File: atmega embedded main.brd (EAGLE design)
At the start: 354.1 x 155.8 mm, 148 parts, among them K1 SWITCH, K10 SWITCH, K11 SWITCH, K12 SWITCH, K13 SWITCH, K14 SWITCH, K15 SWITCH, K16 SWITCH, K17 SWITCH, K18 SWITCH, K19 SWITCH, K2 SWITCH, K20 SWITCH, K21 SWITCH, K22 SWITCH, K23 SWITCH, K24 SWITCH, K25 SWITCH, K26 SWITCH, K27 SWITCH, K28 SWITCH, K29 SWITCH, K3 SWITCH, K30 SWITCH, K31 SWITCH, K32 SWITCH, K33 SWITCH, K34 SWITCH, K35 SWITCH, K36 SWITCH, K37 SWITCH, K38 SWITCH, K39 SWITCH, K4 SWITCH, K40 SWITCH, K41 SWITCH, K42 SWITCH, K43 SWITCH, K44 SWITCH, K45 SWITCH, K46 SWITCH, K47 SWITCH, K48 SWITCH, K49 SWITCH, K5 SWITCH, K50 SWITCH, K51 SWITCH, K52 SWITCH, K53 SWITCH, K54 SWITCH, K55 SWITCH, K56 SWITCH, K57 SWITCH, K58 SWITCH, K59 SWITCH, K6 SWITCH, K60 SWITCH, K61 SWITCH, K62 SWITCH, K63 SWITCH, K64 SWITCH, K65 SWITCH, K66 SWITCH, K7 SWITCH, K8 SWITCH, K9 SWITCH, U1 ATMEGA32U4-AU, X1 XTAL_GND

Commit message: Replaced chip with Atmege328p and made some other adjustments to the schematic
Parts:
- removed D45: (no value), adafruit:DO-1N4148
- removed D63: (no value), adafruit:SMADIODE
- removed K60: SWITCH, keyboard_switch:KAILH_LOW_PROFILE
- added C10, C9: 22p, adafruit:C0805
- added CN2: (no value), adafruit:USB-MINIB
- added D29: (no value), adafruit:SMADIODE
- added IC1: ATMEGA328PROUND, atmega328:DIL28-3-ROUND
- added R5: 10K, adafruit:M0805
- added R6, R7: 22, adafruit:M0805
- added SW2: (no value), adafruit:PUSHBUTTON_SMD_SJ
- added X2: XTAL_GND, adafruit:NX3225
- moved D15 342.0 mm to (-10.8, -114.8), flipped to the top
- moved K47 340.2 mm to (-4.40, -130.4), flipped to the top
- moved K24 147.0 mm to (-4.40, -102.8), flipped to the top
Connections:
- removed net N$43: D45.C, K24.P$2
- removed net N$65: D63.C, K60.P$2
- removed net N$80: D15.C, K47.P$2
- new net D+: CN2.D+, IC1.23, R6.1, R6.2
- new net D-: CN2.D-, R7.2
- new net N$15: IC1.1, R5.2, SW2.P$2
- new net N$16: C9.1, IC1.9, X2.1
- new net N$17: C10.1, IC1.10, X2.3
- new net N$19: D15.C, K24.P$2
- new net N$20: D29.C, K47.P$2
- new net N$21: IC1.24, R7.1
- new net N$22: CN2.ID
- net COL10: now also K62.P$1
- net COL13: no longer K60.P$1
- net COL14: no longer K47.P$1
- net COL3: no longer K24.P$1
- net COL6: now also K47.P$1
- net COL8: now also K24.P$1
- net COL9: no longer K62.P$1
- net G1: now also X2.4
- net GND: now also C10.2, C9.2, CN2.GND, IC1.22, IC1.8, SW2.P$1, X2.2
- net ROW1: now also D15.A, D29.A
- net ROW2: no longer D45.A, D63.A
- net ROW4: no longer D15.A
- net VCC: now also CN2.VBUS, IC1.20, IC1.21, IC1.7, R5.1
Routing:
- net N$80: track 7.45 -> 0.00 mm
- net N$65: track 7.45 -> 0.00 mm
- net N$18: track 7.45 -> 0.00 mm
- net COL2: track 101.4 -> 95.4 mm

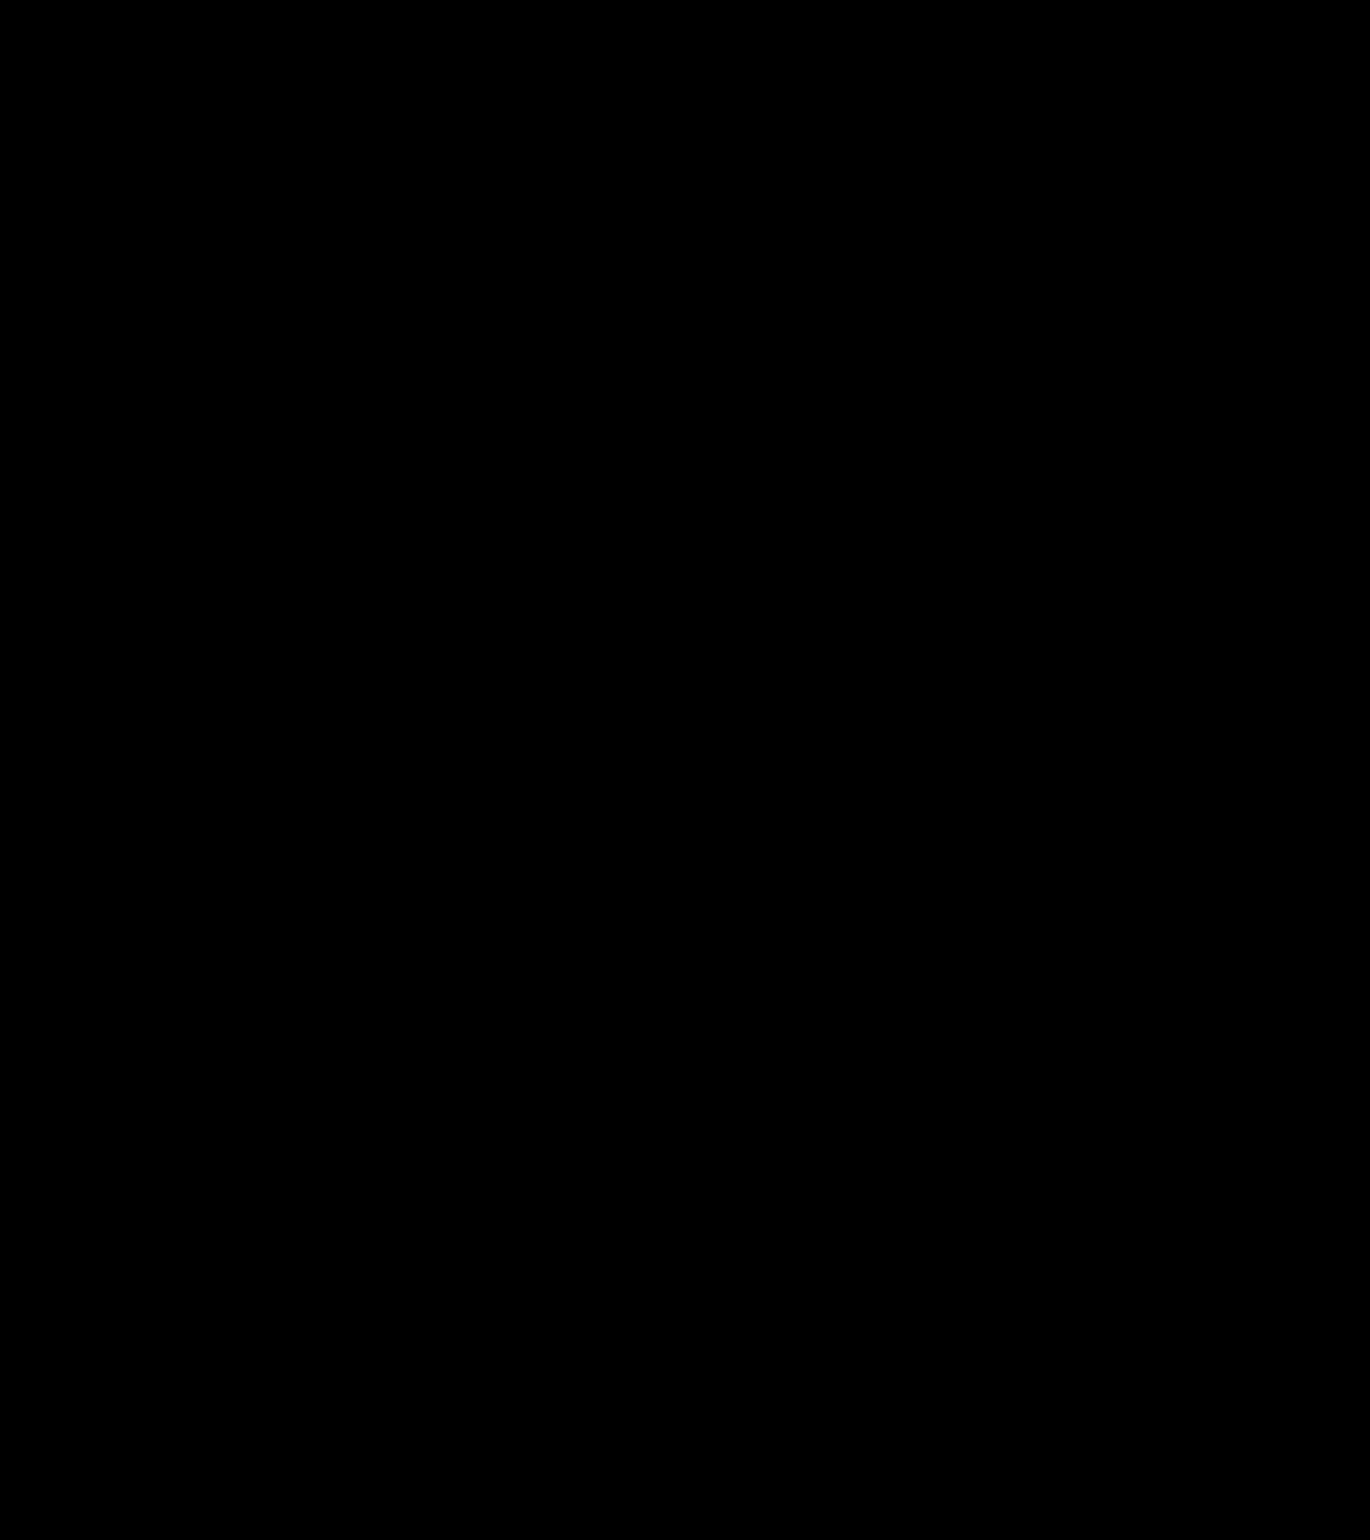
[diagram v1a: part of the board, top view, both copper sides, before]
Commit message: Added an alternative wiring with fake rows for a chip with fewer pins
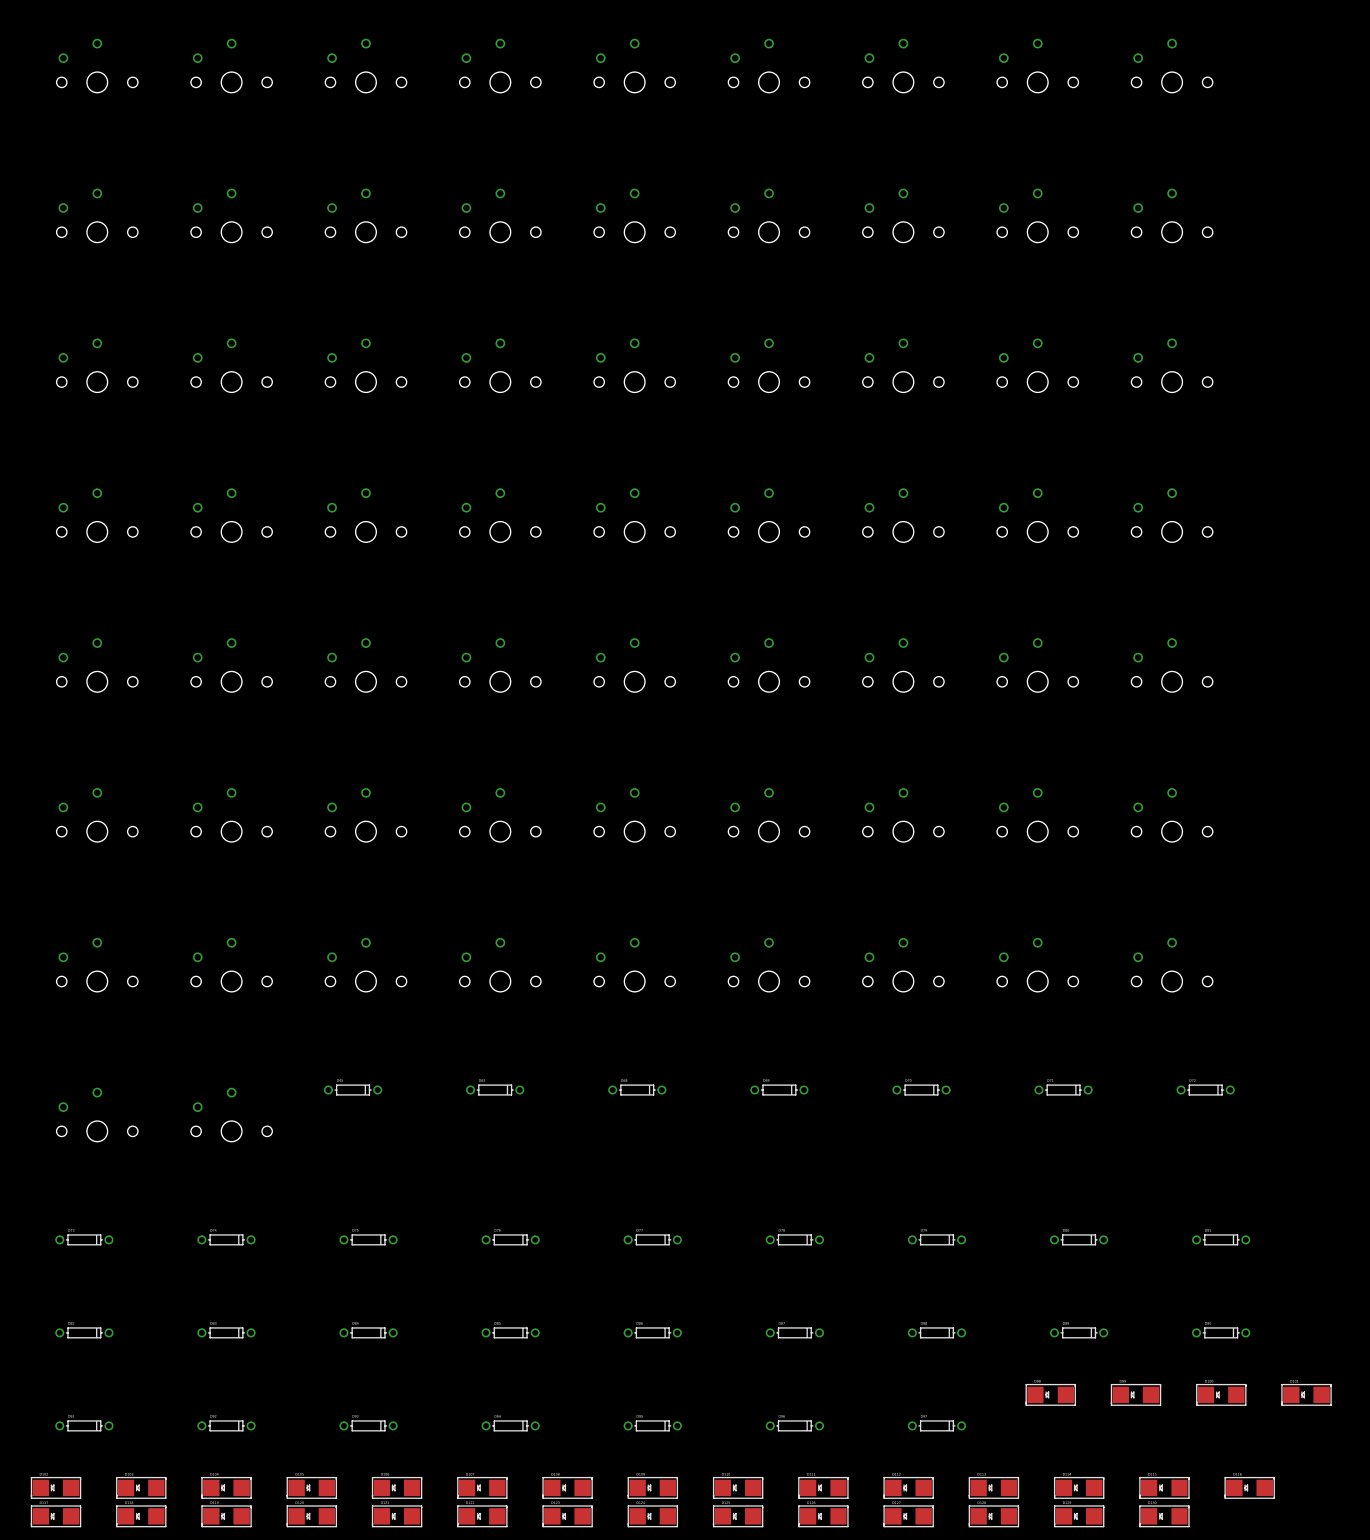
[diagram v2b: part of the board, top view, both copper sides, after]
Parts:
- added D100, D101, D102, D103, D104, D105, D106, D107, D108, D109, D110, D111, D112, D113, D114, D115, D116, D117, D118, D119, D120, D121, D122, D123, D124, D125, D126, D127, D128, D129, D130, D98, D99: (no value), adafruit:SMADIODE
- added D45, D63, D68, D69, D70, D71, D72, D73, D74, D75, D76, D77, D78, D79, D80, D81, D82, D83, D84, D85, D86, D87, D88, D89, D90, D91, D92, D93, D94, D95, D96, D97: (no value), adafruit:DO-1N4148
- added K100, K101, K102, K103, K104, K105, K106, K107, K108, K109, K110, K111, K112, K113, K114, K115, K116, K117, K118, K119, K120, K121, K122, K123, K124, K125, K126, K127, K128, K129, K130, K60, K67, K68, K69, K70, K71, K72, K73, K74, K75, K76, K77, K78, K79, K80, K81, K82, K83, K84, K85, K86, K87, K88, K89, K90, K91, K92, K93, K94, K95, K96, K97, K98, K99: SWITCH, keyboard_switch:KAILH_LOW_PROFILE
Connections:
- new net N$100: D71.C, K71.P$2
- new net N$101: D74.C, K78.P$2
- new net N$102: D116.C, K98.P$1
- new net N$103: D117.C, K105.P$1
- new net N$104: D95.C, K85.P$2
- new net N$105: D94.C, K91.P$2
- new net N$106: D104.C, K128.P$2
- new net N$107: D86.C, K97.P$2
- new net N$108: D93.C, K90.P$2
- new net N$109: D92.C, K84.P$2
- new net N$110: D75.C, K77.P$2
- new net N$111: D115.C, K104.P$2
- new net N$112: D127.C, K123.P$2
- new net N$113: D111.C, K124.P$2
- new net N$114: D126.C, K121.P$2
- new net N$115: D120.C, K120.P$2
- new net N$116: D128.C, K117.P$2
- new net N$118: D114.C, K127.P$2
- new net N$119: D113.C, K126.P$2
- new net N$120: D112.C, K125.P$2
- new net N$121: D119.C, K119.P$2
- new net N$123: D99.C, K99.P$2
- new net N$124: D100.C, K100.P$2
- new net N$125: D101.C, K101.P$2
- new net N$126: D102.C, K102.P$2
- new net N$127: D103.C, K103.P$2
- new net N$130: D124.C, K116.P$2
- new net N$131: D123.C, K115.P$2
- new net N$132: D122.C, K114.P$2
- new net N$133: D121.C, K113.P$2
- new net N$134: D118.C, K112.P$2
- new net N$135: D109.C, K106.P$2
- new net N$136: D108.C, K107.P$2
- new net N$137: D107.C, K108.P$2
- new net N$138: D106.C, K109.P$2
- new net N$139: D105.C, K110.P$2
- new net N$141: D63.C, K67.P$2
- new net N$142: D125.C, K122.P$2
- new net N$143: D129.C, K129.P$1
- new net N$144: D130.C, K130.P$2
- new net N$151: D82.C, K93.P$1
- new net N$152: D81.C, K87.P$1
- new net N$153: D80.C, K80.P$1
- new net N$154: D105.A, D106.A, D107.A, D108.A, D109.A
- new net N$155: D100.A, D101.A, D102.A, D103.A, D99.A
- new net N$160: D87.A, D90.A, D93.A, D94.A
- new net N$161: D72.C, K72.P$2
- new net N$162: D73.C, K79.P$2
- new net N$163: D96.C, K86.P$2
- new net N$164: D97.C, K92.P$2
- new net N$23: D45.C, K60.P$1
- new net N$24: D83.C, K94.P$2
- new net N$25: D79.C, K73.P$1
- new net N$26: D118.A, D121.A, D122.A, D123.A, D124.A
- new net N$27: D98.C, K118.P$1
- new net N$28: D110.C, K111.P$1
- new net N$35: D78.C, K74.P$2
- new net N$43: D77.C, K75.P$2
- new net N$64: D68.C, K68.P$2
- new net N$65: D89.C, K82.P$2
- new net N$72: D88.C, K81.P$2
- new net N$80: D87.C, K88.P$2
- new net N$92: D84.C, K95.P$2
- new net N$93: D85.C, K96.P$2
- new net N$94: D90.C, K89.P$2
- new net N$95: D91.C, K83.P$2
- new net N$96: D76.C, K76.P$2
- new net N$97: D69.C, K69.P$2
- new net N$98: D70.C, K70.P$2
- new net ROW6: D104.A, D115.A, D127.A, D128.A, D45.A, D79.A, D80.A, D81.A, D82.A
- new net ROW7: D110.A, D116.A, D117.A, D72.A, D73.A, D96.A, D97.A, D98.A
- net COL10: now also K100.P$1, K107.P$1, K111.P$2, K113.P$1, K120.P$1, K124.P$1, K128.P$1
- net COL11: now also K101.P$1, K105.P$2, K108.P$1, K114.P$1, K121.P$1, K123.P$1, K125.P$1
- net COL12: now also K102.P$1, K109.P$1, K115.P$1, K117.P$1, K122.P$1, K126.P$1, K98.P$2
- net COL13: now also K103.P$1, K104.P$1, K110.P$1, K116.P$1, K127.P$1
- net COL2: now also K60.P$2, K67.P$1, K74.P$1, K81.P$1, K88.P$1, K94.P$1
- net COL3: now also K68.P$1, K72.P$1, K73.P$2, K75.P$1, K82.P$1, K95.P$1
- net COL4: now also K69.P$1, K76.P$1, K79.P$1, K80.P$2, K83.P$1, K89.P$1, K96.P$1
- net COL5: now also K70.P$1, K77.P$1, K84.P$1, K86.P$1, K87.P$2, K90.P$1, K97.P$1
- net COL6: now also K130.P$1, K71.P$1, K78.P$1, K85.P$1, K91.P$1, K92.P$1, K93.P$2
- net COL9: now also K106.P$1, K112.P$1, K118.P$2, K119.P$1, K129.P$2, K99.P$1
- net ROW1: now also D63.A, D68.A, D69.A, D70.A, D71.A
- net ROW2: now also D74.A, D75.A, D76.A, D77.A, D78.A
- net ROW3: now also D88.A, D89.A, D91.A, D92.A, D95.A
- net ROW4: now also D119.A, D120.A, D125.A, D126.A
- net ROW5: now also D111.A, D112.A, D113.A, D114.A, D129.A, D130.A, D83.A, D84.A, D85.A, D86.A

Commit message: Traced stuff
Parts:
- removed C1, C2: 22p, adafruit:C0805
- removed C8: 1u, adafruit:C0805
- removed CN1, CN2: (no value), adafruit:USB-MINIB
- removed D1, D2, D22, D23, D24, D25, D26, D27, D28, D3, D30, D31, D32, D33, D34, D35, D36, D4, D42, D43, D44, D46, D47, D48, D49, D5, D50, D51, D52, D53, D6, D7: (no value), adafruit:DO-1N4148
- removed D10, D11, D12, D13, D14, D15, D16, D17, D18, D19, D20, D21, D29, D37, D38, D39, D40, D41, D54, D55, D56, D57, D58, D59, D60, D61, D62, D64, D65, D66, D67, D8, D9: (no value), adafruit:SMADIODE
- removed K1, K10, K11, K12, K13, K14, K15, K16, K17, K18, K19, K2, K20, K21, K22, K23, K24, K25, K26, K27, K28, K29, K3, K30, K31, K32, K33, K34, K35, K36, K37, K38, K39, K4, K40, K41, K42, K43, K44, K45, K46, K47, K48, K49, K5, K50, K51, K52, K53, K54, K55, K56, K57, K58, K59, K6, K61, K62, K63, K64, K65, K66, K7, K8, K9: SWITCH, keyboard_switch:KAILH_LOW_PROFILE
- removed R1, R2: 10K, adafruit:M0805
- removed R3, R4: 22, adafruit:M0805
- removed SW1, SW2: (no value), adafruit:PUSHBUTTON_SMD_SJ
- removed X1, X2: XTAL_GND, adafruit:NX3225
- added Q1: (no value), crystal:HC49/S
- added S1: (no value), switch-omron:B3F-10XX
- D45, D63, D68, D69, D70, D71, D72, D73, D74, D75, D76, D77, D78, D79, D80, D81, D82, D83, D84, D85, D86, D87, D88, D89, D90, D91, D92, D93, D94, D95, D96, D97: device adafruit:DO-1N4148 -> adafruit:SMADIODE
- U1: value ATMEGA32U4-AU -> (none); device adafruit:TQFP44 -> microusb:USB-MICRO-SMD
- moved D103 540.0 mm to (271.9, 80.8)
- moved D102 537.7 mm to (254.1, 80.8)
- moved D105 510.8 mm to (272.5, 61.8)
- moved D106 496.5 mm to (254.1, 61.8)
- moved D117 490.7 mm to (165.1, 66.5), turned to 180 degrees
- moved D115 489.7 mm to (288.6, 85.5), turned to 180 degrees
- moved D107 483.7 mm to (235.1, 61.8)
- moved D104 481.5 mm to (288.6, 9.50), turned to 180 degrees
- moved D118 476.0 mm to (197.1, 42.8)
- moved D124 474.5 mm to (272.5, 42.8)
- moved D128 474.4 mm to (288.6, 57.0), turned to 180 degrees
- moved D116 472.8 mm to (165.1, 85.5), turned to 180 degrees
- moved D108 472.6 mm to (216.1, 61.8)
- moved D123 472.4 mm to (254.1, 42.8)
- moved D122 470.1 mm to (235.1, 42.8)
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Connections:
- removed net COL11: K101.P$1, K105.P$2, K108.P$1, K114.P$1, K121.P$1, K123.P$1, K125.P$1, K37.P$1, K44.P$1, K51.P$1, K58.P$1, K63.P$1, U1.12
- removed net COL12: K102.P$1, K109.P$1, K115.P$1, K117.P$1, K122.P$1, K126.P$1, K38.P$1, K45.P$1, K52.P$1, K59.P$1, K64.P$1, K98.P$2, U1.36
- removed net COL13: K103.P$1, K104.P$1, K110.P$1, K116.P$1, K127.P$1, K39.P$1, K46.P$1, K53.P$1, K65.P$1, U1.37
- removed net COL14: K40.P$1, K54.P$1, K61.P$1, K66.P$1, U1.38
- removed net G1: X1.4, X2.4
- removed net N$1 (its old number): C1.1, U1.17, X1.1
- removed net N$100: D71.C, K71.P$2
- removed net N$101: D74.C, K78.P$2
- removed net N$102: D116.C, K98.P$1
- removed net N$103: D117.C, K105.P$1
- removed net N$104: D95.C, K85.P$2
- removed net N$105: D94.C, K91.P$2
- removed net N$107: D86.C, K97.P$2
- removed net N$108: D93.C, K90.P$2
- removed net N$109: D92.C, K84.P$2
- removed net N$110: D75.C, K77.P$2
- removed net N$113: D111.C, K124.P$2
- removed net N$114: D126.C, K121.P$2
- removed net N$115: D120.C, K120.P$2
- removed net N$118: D114.C, K127.P$2
- removed net N$119: D113.C, K126.P$2
- removed net N$120: D112.C, K125.P$2
- removed net N$121: D119.C, K119.P$2
- removed net N$123: D99.C, K99.P$2
- removed net N$124: D100.C, K100.P$2
- removed net N$125: D101.C, K101.P$2
- removed net N$126: D102.C, K102.P$2
- removed net N$127: D103.C, K103.P$2
- removed net N$130: D124.C, K116.P$2
- removed net N$131: D123.C, K115.P$2
- removed net N$132: D122.C, K114.P$2
- removed net N$133: D121.C, K113.P$2
- removed net N$134: D118.C, K112.P$2
- removed net N$135: D109.C, K106.P$2
- removed net N$136: D108.C, K107.P$2
- removed net N$137: D107.C, K108.P$2
- removed net N$138: D106.C, K109.P$2
- removed net N$139: D105.C, K110.P$2
- removed net N$141: D63.C, K67.P$2
- removed net N$144: D130.C, K130.P$2
- removed net N$154: D105.A, D106.A, D107.A, D108.A, D109.A
- removed net N$155: D100.A, D101.A, D102.A, D103.A, D99.A
- removed net N$160: D87.A, D90.A, D93.A, D94.A
- removed net N$161: D72.C, K72.P$2
- removed net N$162: D73.C, K79.P$2
- removed net N$163: D96.C, K86.P$2
- removed net N$164: D97.C, K92.P$2
- removed net N$2 (its old number): C2.1, U1.16, X1.3
- removed net N$26 (its old number): D118.A, D121.A, D122.A, D123.A, D124.A
- removed net N$3 (its old number): R1.2, SW1.P$2, U1.13
- removed net N$4 (its old number): R2.2, U1.33
- removed net N$42: D34.C, K31.P$2
- removed net N$5 (its old number): CN1.D+, R3.1
- removed net N$65 (its old number): D89.C, K82.P$2
- removed net N$66 (its old number): D67.C, K61.P$2
- removed net N$67 (its old number): D41.C, K66.P$2
- removed net N$68 (its old number): D40.C, K65.P$2
- removed net N$69: D39.C, K64.P$2
- removed net N$70: D38.C, K63.P$2
- removed net N$71: D57.C, K56.P$2
- removed net N$72: D88.C, K81.P$2
- removed net N$73: D21.C, K41.P$2
- removed net N$74: D9.C, K35.P$2
- removed net N$75: D10.C, K36.P$2
- removed net N$76: D11.C, K37.P$2
- removed net N$77: D12.C, K38.P$2
- removed net N$78: D13.C, K39.P$2
- removed net N$79: D14.C, K40.P$2
- removed net N$81: D66.C, K54.P$2
- removed net N$82: D62.C, K53.P$2
- removed net N$83: D61.C, K52.P$2
- removed net N$84: D60.C, K51.P$2
- removed net N$85: D59.C, K50.P$2
- removed net N$86: D56.C, K49.P$2
- removed net N$87: D20.C, K42.P$2
- removed net N$88: D19.C, K43.P$2
- removed net N$89: D18.C, K44.P$2
- removed net N$90: D17.C, K45.P$2
- removed net N$91: D16.C, K46.P$2
- removed net N$92: D84.C, K95.P$2
- removed net N$93: D85.C, K96.P$2
- removed net N$94: D90.C, K89.P$2
- removed net N$95: D91.C, K83.P$2
- removed net N$96: D76.C, K76.P$2
- removed net N$97: D69.C, K69.P$2
- removed net N$98: D70.C, K70.P$2
- new net N$23: D86.C, K97.P$1
- new net N$25: D75.C, K77.P$1
- net COL1: now also K60.P$2, K67.P$2, K74.P$2, K81.P$2, K88.P$2, K94.P$2; no longer K1.P$1, K15.P$1, K22.P$1, K29.P$1, K8.P$1, U1.22
- net COL10: now also K103.P$2, K104.P$1, K110.P$2, K116.P$2, K127.P$2; no longer K100.P$1, K107.P$1, K111.P$2, K113.P$1, K120.P$1, K124.P$1, K128.P$1, K36.P$1, K43.P$1, K50.P$1, K57.P$1, K62.P$1, U1.30
- net COL2: now also K68.P$2, K72.P$2, K73.P$2, K75.P$2, K82.P$2, K95.P$2; no longer K16.P$1, K2.P$1, K23.P$1, K30.P$1, K60.P$2, K67.P$1, K74.P$1, K81.P$1, K88.P$1, K9.P$1, K94.P$1, U1.21
- net COL3: now also K69.P$2, K76.P$2, K79.P$2, K80.P$2, K83.P$2, K89.P$2, K96.P$2; no longer K10.P$1, K17.P$1, K3.P$1, K31.P$1, K68.P$1, K72.P$1, K73.P$2, K75.P$1, K82.P$1, K95.P$1, U1.20
- net COL4: now also K70.P$2, K77.P$2, K84.P$2, K86.P$2, K87.P$2, K90.P$2, K97.P$2; no longer K11.P$1, K18.P$1, K25.P$1, K32.P$1, K4.P$1, K69.P$1, K76.P$1, K79.P$1, K80.P$2, K83.P$1, K89.P$1, K96.P$1, U1.8
- net COL5: now also K130.P$2, K71.P$2, K78.P$2, K85.P$2, K91.P$2, K92.P$2, K93.P$2; no longer K12.P$1, K19.P$1, K26.P$1, K33.P$1, K5.P$1, K70.P$1, K77.P$1, K84.P$1, K86.P$1, K87.P$2, K90.P$1, K97.P$1, U1.9
- net COL6: now also K106.P$2, K112.P$2, K118.P$1, K119.P$2, K129.P$2, K99.P$2; no longer K13.P$1, K130.P$1, K20.P$1, K27.P$1, K47.P$1, K6.P$1, K71.P$1, K78.P$1, K85.P$1, K91.P$1, K92.P$1, K93.P$2, U1.10
- net COL7: now also K100.P$2, K107.P$2, K111.P$1, K113.P$2, K120.P$2, K124.P$2, K128.P$1; no longer K14.P$1, K21.P$1, K28.P$1, K7.P$1, U1.11
- net COL8: now also K101.P$2, K105.P$1, K108.P$2, K114.P$2, K121.P$2, K123.P$1, K125.P$2; no longer K24.P$1, K34.P$1, K41.P$1, K48.P$1, K55.P$1, U1.19
- net COL9: now also K102.P$2, K109.P$2, K115.P$2, K117.P$1, K122.P$2, K126.P$2, K98.P$1; no longer K106.P$1, K112.P$1, K118.P$2, K119.P$1, K129.P$2, K35.P$1, K42.P$1, K49.P$1, K56.P$1, K99.P$1, U1.18
- net D+: now also U1.D+1; no longer CN2.D+
- net D-: now also U1.D-1; no longer CN2.D-
- net GND: now also S1.4, U1.GND1; no longer C1.2, C2.2, C8.1, CN1.GND, CN2.GND, R2.1, SW1.P$1, SW2.P$1, U1.15, U1.23, U1.35, U1.43, U1.5, X1.2, X2.2
- net N$10: now also D77.C, K75.P$1; no longer D49.C, K26.P$2
- net N$11: now also D89.C, K82.P$1; no longer D48.C, K19.P$2
- net N$12: now also D68.C, K68.P$1; no longer D24.C, K12.P$2
- net N$13: now also D84.C, K95.P$1; no longer D8.C, K34.P$2
- net N$14: now also D76.C, K76.P$1; no longer D2.C, K2.P$2
- net N$142: now also K122.P$1; no longer K122.P$2
- net N$15: now also S1.1, S1.2; no longer SW2.P$2
- net N$16: now also Q1.2; no longer X2.1
- net N$17: now also Q1.1; no longer X2.3
- net N$18: now also D69.C, K69.P$1; no longer D64.C, K59.P$2
- net N$19: now also D90.C, K89.P$1; no longer D15.C, K24.P$2
- net N$20: now also D85.C, K96.P$1; no longer D29.C, K47.P$2
- net N$22: now also D91.C, K83.P$1; no longer CN2.ID
- net N$24: now also D70.C, K70.P$1; no longer D83.C, K94.P$2
- net N$27: now also K118.P$2; no longer K118.P$1
- net N$28: now also K111.P$2; no longer K111.P$1
- net N$29: now also D92.C, K84.P$1; no longer D32.C, K29.P$2
- net N$30: now also D93.C, K90.P$1; no longer D33.C, K30.P$2
- net N$31: now also D94.C, K91.P$1; no longer D31.C, K22.P$2
- net N$32: now also D71.C, K71.P$1; no longer D30.C, K15.P$2
- net N$33: now also D74.C, K78.P$1; no longer D28.C, K8.P$2
- net N$34: now also D95.C, K85.P$1; no longer D1.C, K1.P$2
- net N$35: now also D130.C, K130.P$1; no longer D78.C, K74.P$2
- net N$36: now also D72.C, K72.P$1; no longer D27.C, K9.P$2
- net N$37: now also D73.C, K79.P$1; no longer D26.C, K10.P$2
- net N$38: now also D96.C, K86.P$1; no longer D3.C, K3.P$2
- net N$39: now also D97.C, K92.P$1; no longer D44.C, K17.P$2
- net N$40: now also D117.C, K105.P$2; no longer D43.C, K16.P$2
- net N$41: now also D116.C, K98.P$2; no longer D42.C, K23.P$2
- net N$43: now also D119.C, K119.P$1; no longer D77.C, K75.P$2
- net N$44: now also D99.C, K99.P$1; no longer D35.C, K32.P$2
- net N$45: now also D109.C, K106.P$1; no longer D46.C, K25.P$2
- net N$46: now also D118.C, K112.P$1; no longer D47.C, K18.P$2
- net N$47: now also D111.C, K124.P$1; no longer D25.C, K11.P$2
- net N$48: now also D100.C, K100.P$1; no longer D4.C, K4.P$2
- net N$49: now also D108.C, K107.P$1; no longer D5.C, K5.P$2
- net N$50: now also D121.C, K113.P$1; no longer D7.C, K7.P$2
- net N$51: now also D120.C, K120.P$1; no longer D6.C, K6.P$2
- net N$52: now also D126.C, K121.P$1; no longer D23.C, K13.P$2
- net N$53: now also D101.C, K101.P$1; no longer D22.C, K14.P$2
- net N$54: now also D107.C, K108.P$1; no longer D52.C, K21.P$2
- net N$55: now also D122.C, K114.P$1; no longer D51.C, K20.P$2
- net N$56: now also D112.C, K125.P$1; no longer D50.C, K27.P$2
- net N$57: now also D123.C, K115.P$1; no longer D53.C, K28.P$2
- net N$58: now also D106.C, K109.P$1; no longer D54.C, K55.P$2
- net N$59: now also D102.C, K102.P$1; no longer D55.C, K48.P$2
- net N$6: now also D63.C, K67.P$1; no longer CN1.D-, R4.1
- net N$60: now also D113.C, K126.P$1; no longer D36.C, K33.P$2
- net N$61: now also D124.C, K116.P$1; no longer D37.C, K62.P$2
- net N$62: now also D105.C, K110.P$1; no longer D65.C, K58.P$2
- net N$63: now also D103.C, K103.P$1; no longer D58.C, K57.P$2
- net N$64: now also D114.C, K127.P$1; no longer D68.C, K68.P$2
- net N$7: now also D88.C, K81.P$1; no longer R4.2, U1.3
- net N$8: now also D78.C, K74.P$1; no longer R3.2, U1.4
- net N$80: now also K88.P$1; no longer K88.P$2
- net N$9: now also D83.C, K94.P$1; no longer C8.2, U1.6
- net ROW1: now also D100.A, D101.A, D102.A, D103.A, D99.A; no longer D15.A, D29.A, D32.A, D33.A, D34.A, D35.A, D36.A, D37.A, D38.A, D39.A, D40.A, D41.A, U1.29
- net ROW2: now also D105.A, D106.A, D107.A, D108.A, D109.A; no longer D31.A, D42.A, D46.A, D49.A, D50.A, D53.A, D54.A, D57.A, D58.A, D64.A, D65.A, D67.A, U1.28
- net ROW3: now also D118.A, D121.A, D122.A, D123.A, D124.A; no longer D30.A, D43.A, D44.A, D47.A, D48.A, D51.A, D52.A, D55.A, D56.A, D59.A, D60.A, D61.A, D62.A, D66.A, U1.27
- net ROW4: now also D87.A, D90.A, D93.A, D94.A; no longer D16.A, D17.A, D18.A, D19.A, D20.A, D21.A, D22.A, D23.A, D24.A, D25.A, D26.A, D27.A, D28.A, U1.26
- net ROW5: no longer D1.A, D10.A, D11.A, D12.A, D13.A, D14.A, D2.A, D3.A, D4.A, D5.A, D6.A, D7.A, D8.A, D9.A, U1.25
- net VCC: now also U1.VBUS1; no longer CN1.VBUS, CN2.VBUS, R1.1, U1.14, U1.2, U1.24, U1.34, U1.44
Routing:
- net ROW3: track 0.00 -> 369.7 mm
- net ROW5: track 114.2 -> 479.1 mm
- net ROW4: track 38.4 -> 389.8 mm, vias 2 -> 0
- net ROW2: track 0.00 -> 330.0 mm
- net ROW1: track 0.00 -> 262.2 mm
- net ROW6: track 0.00 -> 170.5 mm
- net ROW7: track 0.00 -> 119.7 mm
- net COL10: track 0.00 -> 110.5 mm
- net COL9: track 0.00 -> 109.5 mm
- net COL8: track 0.00 -> 104.0 mm
- net COL5: track 9.40 -> 111.2 mm, vias 1 -> 0
- net COL6: track 9.40 -> 104.4 mm, vias 1 -> 0
- net COL7: track 9.40 -> 104.0 mm, vias 1 -> 0
- net COL3: track 9.40 -> 104.0 mm, vias 1 -> 0
- net COL4: track 9.50 -> 104.0 mm, vias 1 -> 0
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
